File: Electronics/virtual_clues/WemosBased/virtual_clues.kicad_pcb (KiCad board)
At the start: 2 copper layers, 61 x 70 mm, 26 parts, among them Q1 IRLB8721PBF, U1 L7805

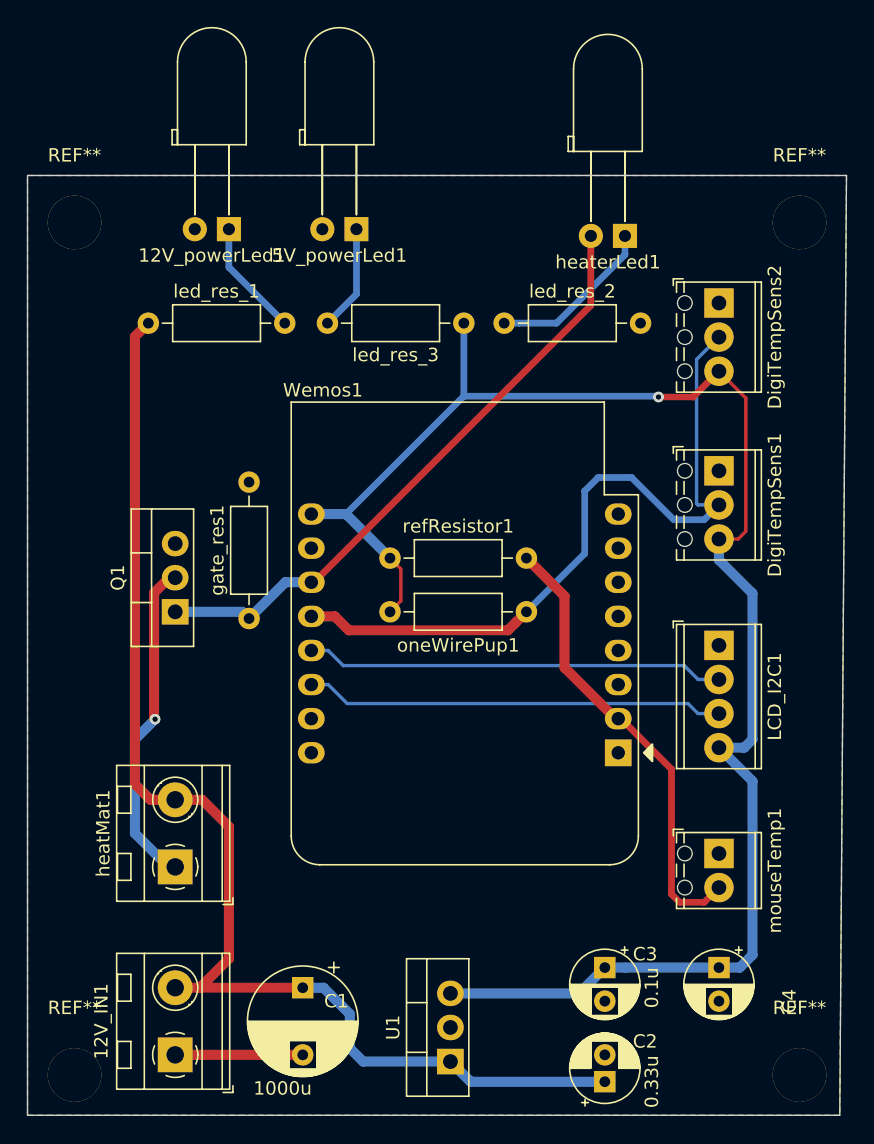
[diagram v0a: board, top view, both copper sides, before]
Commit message: update PCB for 3rd temp sensor and additional heat pad + better labels
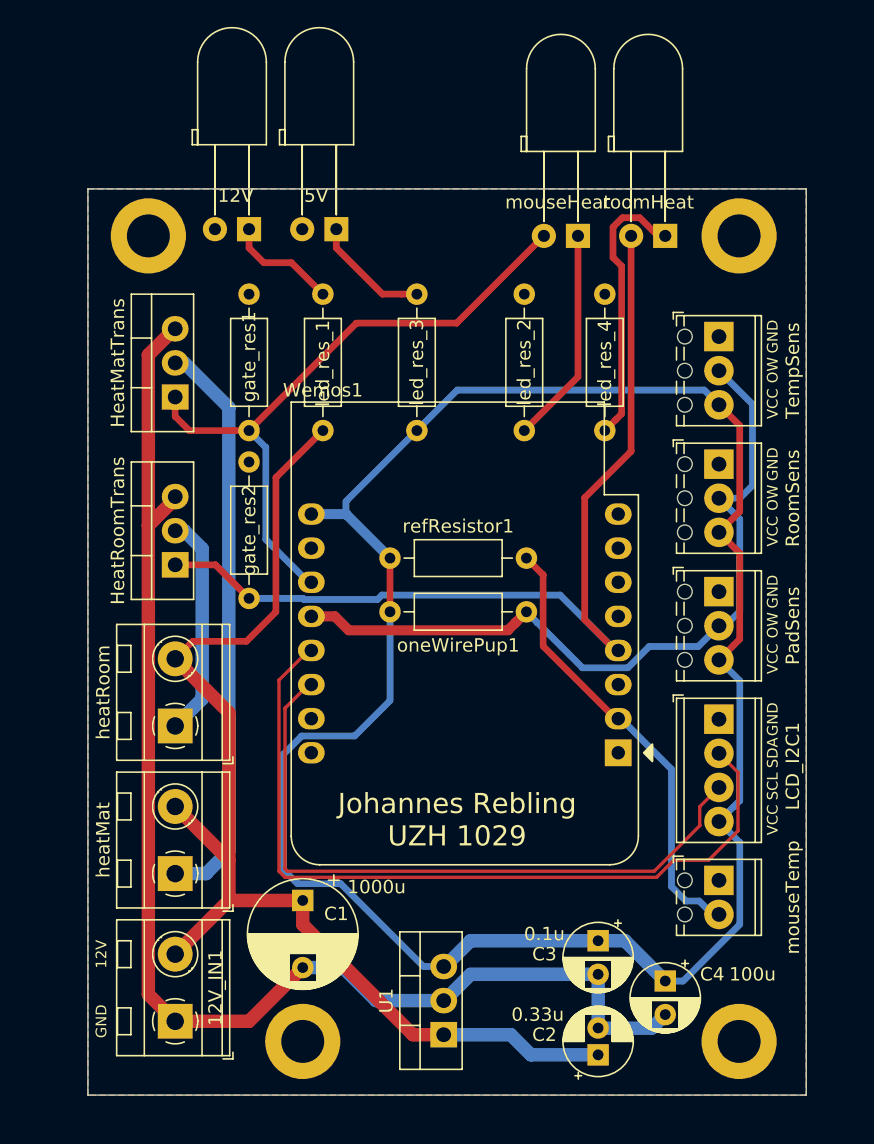
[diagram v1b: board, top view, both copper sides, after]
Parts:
- removed Q1: IRLB8721PBF, Package_TO_SOT_THT:TO-220-3_Vertical
- removed REF** (x4): MountingHole_4mm, MountingHole:MountingHole_4mm
- removed heaterLed1: heaterLed, LED_THT:LED_D5.0mm_Horizontal_O6.35mm_Z3.0mm
- added ?: MountingHole_3.2mm_M3_DIN965_Pad, MountingHole:MountingHole_3.2mm_M3_DIN965_Pad, F.Cu at (88.0, 103.0)
- added ?: MountingHole_3.2mm_M3_DIN965_Pad, MountingHole:MountingHole_3.2mm_M3_DIN965_Pad, F.Cu at (76.5, 43.0)
- added ?: MountingHole_3.2mm_M3_DIN965_Pad, MountingHole:MountingHole_3.2mm_M3_DIN965_Pad, F.Cu at (120.5, 103.0)
- added ?: MountingHole_3.2mm_M3_DIN965_Pad, MountingHole:MountingHole_3.2mm_M3_DIN965_Pad, F.Cu at (120.5, 43.0)
- added HeatMatTrans: IRLB8721PBF, Package_TO_SOT_THT:TO-220-3_Vertical, F.Cu at (78.5, 55.0)
- added HeatRoomTrans: IRLB8721PBF, Package_TO_SOT_THT:TO-220-3_Vertical, F.Cu at (78.5, 67.5)
- added TempSens: DigiTempSens2, TerminalBlock_Phoenix:TerminalBlock_Phoenix_MPT-0,5-3-2.54_1x03_P2.54mm_Horizontal, F.Cu at (119.0, 50.5)
- added gate_res2: 10k, Resistor_THT:R_Axial_DIN0207_L6.3mm_D2.5mm_P10.16mm_Horizontal, F.Cu at (84.0, 70.0)
- added heatRoom: heatMat1, TerminalBlock_MetzConnect:TerminalBlock_MetzConnect_Type094_RT03502HBLU_1x02_P5.00mm_Horizontal, F.Cu at (78.5, 79.5)
- added led_res_4: 150, Resistor_THT:R_Axial_DIN0207_L6.3mm_D2.5mm_P10.16mm_Horizontal, F.Cu at (110.5, 57.5)
- added mouseHeat: heaterLed, LED_THT:LED_D5.0mm_Horizontal_O6.35mm_Z3.0mm, F.Cu at (108.5, 43.0)
- added roomHeat: heaterLed, LED_THT:LED_D5.0mm_Horizontal_O6.35mm_Z3.0mm, F.Cu at (115.0, 43.0)
- moved led_res_1 15.3 mm to (89.5, 57.5), turned to 90 degrees
- moved gate_res1 14.0 mm to (84.0, 57.5)
- moved RoomSens 12.0 mm to (119.0, 60.0)
- moved PadSens 9.00 mm to (119.0, 69.5)
- moved led_res_3 8.73 mm to (96.5, 57.5), turned to 90 degrees
- moved led_res_2 8.14 mm to (104.5, 57.5), turned to 90 degrees
- moved C1 6.50 mm to (88.0, 92.5)
- moved LCD_I2C1 5.50 mm to (119.0, 79.0)
- moved C4 4.12 mm to (115.0, 98.5)
- moved 12V_IN1 2.50 mm to (78.5, 101.5)
- moved C2 2.06 mm to (110.0, 104.0)
- moved C3 2.06 mm to (110.0, 95.5)
- moved U1 2.06 mm to (98.5, 102.5)
- moved mouseTemp 2.00 mm to (119.0, 91.0)
- moved 12V 1.50 mm to (84.0, 42.5)
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- renumbered 12V_powerLed1 to 12V, 5V_powerLed1 to 5V, DigiTempSens1 to PadSens, DigiTempSens2 to RoomSens, heatMat1 to heatMat, mouseTemp1 to mouseTemp
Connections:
- Wemos1 pad 4: Net-(Wemos1-Pad4) -> HeatRoom
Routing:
- net GND: track 9.50 -> 100.7 mm
- net HeatRoom: track 0.00 -> 69.4 mm
- net VCC: track 123.4 -> 152.6 mm, vias 1 -> 0
- net SDA: track 31.3 -> 59.9 mm
- net Net-(led_res_4-Pad1): track 0.00 -> 20.7 mm
- net SCL: track 31.3 -> 50.5 mm
- net Net-(Q1-Pad2): track 24.6 -> 43.1 mm, vias 1 -> 0
- net Net-(Q2-Pad2): track 0.00 -> 16.6 mm
- net +12V: track 92.4 -> 88.2 mm
- net Net-(heaterLed1-Pad1): track 12.5 -> 16.2 mm
- net OneWireBus: track 54.8 -> 57.9 mm
- net HeatPadCtr: track 46.0 -> 48.7 mm
- net Net-(5V_powerLed1-Pad1): track 7.89 -> 8.82 mm
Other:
- board size 61 x 70 mm -> 53.5 x 67.5 mm
- board text added: "12V"
- board text added: "GND"
- board text added: "Johannes Rebling UZH 1029"
- board text added: "OW"
- board text added: "SCL"
- board text added: "SDA"
- board text added: "VCC"
